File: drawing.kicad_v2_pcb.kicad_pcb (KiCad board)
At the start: 2 copper layers, 93 x 65 mm, 40 parts, among them IC1 DW01A-G, J1 Micro USB Chargeport, J2 Prog headers, J3 128x32 I2C OLED, J4 TP4056, J5 MK-12C02, J6 Conn_01x02, Q1 FS8205, U1 HT7333-SOT89, U2 ESP-12E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

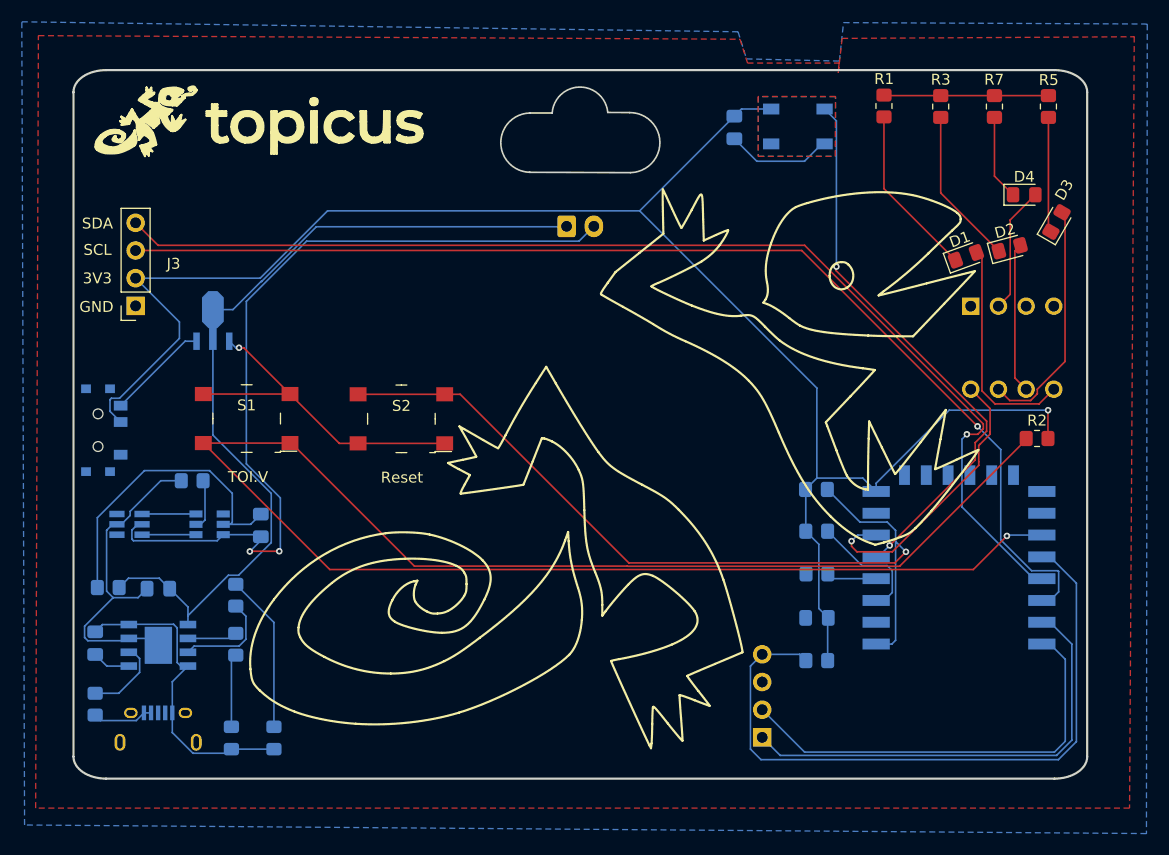
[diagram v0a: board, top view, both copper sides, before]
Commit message: Fixed HT7333 and charging circuit
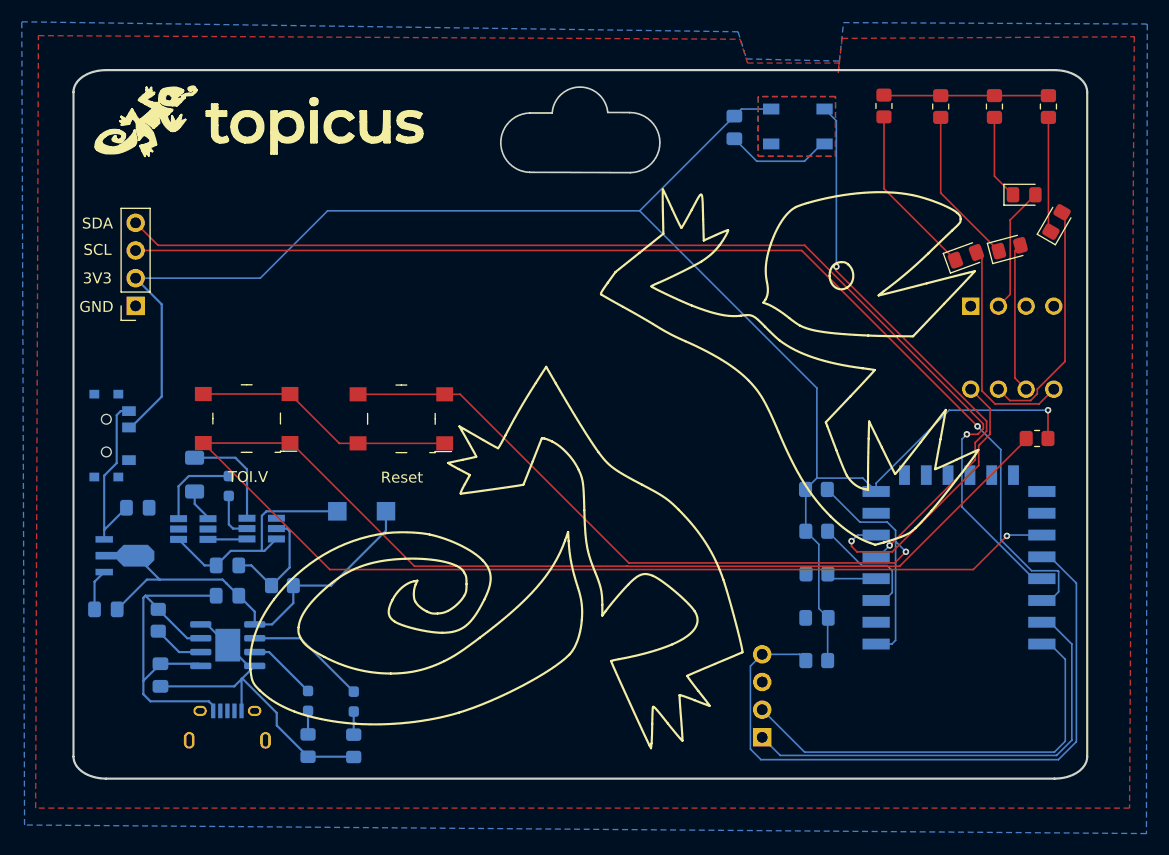
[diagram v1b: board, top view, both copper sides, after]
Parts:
- removed C2, C4: 0.1uF, Capacitor_SMD:C_0805_2012Metric_Pad1.18x1.45mm_HandSolder
- removed C5: 10uF, Capacitor_SMD:C_0805_2012Metric_Pad1.18x1.45mm_HandSolder
- removed D5: R-LED, LED_SMD:LED_0805_2012Metric_Pad1.15x1.40mm_HandSolder
- removed D6: G-LED, LED_SMD:LED_0805_2012Metric_Pad1.15x1.40mm_HandSolder
- removed IC1: DW01A-G, user-footprints:SOT95P280X135-6N
- removed J1: Micro USB Chargeport, digikey-footprints:USB_Micro_B_Female_10118194-0001LF
- removed J4: TP4056, Custom:SOIC127P600X175-9N
- removed J5: MK-12C02, user-footprints:MK12C02
- removed J6: Conn_01x02, Connector_JST:JST_EH_B2B-EH-A_1x02_P2.50mm_Vertical
- removed Q1: FS8205, user-footprints:FS8205
- removed R10, R12, R13: 1k, Resistor_SMD:R_0805_2012Metric_Pad1.20x1.40mm_HandSolder
- removed R11: 5k, Resistor_SMD:R_0805_2012Metric_Pad1.20x1.40mm_HandSolder
- removed R14: 100R, Resistor_SMD:R_0805_2012Metric_Pad1.20x1.40mm_HandSolder
- removed U1: HT7333-SOT89, Custom:Holtek-HT7333-SOT89-Level_A
- added C10: 10uF, Capacitor_SMD:C_0805_2012Metric_Pad1.18x1.45mm_HandSolder, B.Cu at (111.9, 101.6)
- added C6: 0.1uF, Capacitor_SMD:C_0805_2012Metric_Pad1.18x1.45mm_HandSolder, B.Cu at (114.0, 116.9)
- added C7: 10uF, Capacitor_SMD:C_0805_2012Metric_Pad1.18x1.45mm_HandSolder, B.Cu at (120.1, 109.7)
- added C8: 0.1uF, Capacitor_SMD:C_0805_2012Metric_Pad1.18x1.45mm_HandSolder, B.Cu at (120.1, 106.9)
- added C9: 10uF, Capacitor_SMD:C_0805_2012Metric_Pad1.18x1.45mm_HandSolder, B.Cu at (109.0, 110.9)
- added D8: RED, LED_SMD:LED_0805_2012Metric_Pad1.15x1.40mm_HandSolder, B.Cu at (127.5, 123.4)
- added D9: GREEN, LED_SMD:LED_0805_2012Metric_Pad1.15x1.40mm_HandSolder, B.Cu at (131.7, 123.4)
- added J10: Conn_01x01_Female, user-footprints:solderpad, B.Cu at (130.2, 101.9)
- added J12: Conn_01x01_Female, user-footprints:solderpad, B.Cu at (134.7, 101.9)
- added J14: MK-12C02, user-footprints:MK12C02, B.Cu at (109.0, 95.0)
- added J7: USB_B_Micro, digikey-footprints:USB_Micro_B_Female_10118194-0001LF, B.Cu at (120.1, 120.2)
- added R15: 1k, Resistor_SMD:R_0603_1608Metric_Pad0.98x0.95mm_HandSolder, B.Cu at (127.5, 119.3)
- added R16: 1k, Resistor_SMD:R_0603_1608Metric_Pad0.98x0.95mm_HandSolder, B.Cu at (131.7, 119.4)
- added R17: 10k, Resistor_SMD:R_0805_2012Metric_Pad1.20x1.40mm_HandSolder, B.Cu at (113.8, 111.9)
- added R18: 1k, Resistor_SMD:R_0603_1608Metric_Pad0.98x0.95mm_HandSolder, B.Cu at (120.3, 99.6)
- added R19: 0R, Resistor_SMD:R_1206_3216Metric_Pad1.30x1.75mm_HandSolder, B.Cu at (117.1, 98.5)
- added R20: 100, Resistor_SMD:R_0805_2012Metric_Pad1.20x1.40mm_HandSolder, B.Cu at (125.2, 108.7)
- added U4: TP4056, Package_SO:SOIC-8-1EP_3.9x4.9mm_P1.27mm_EP2.29x3mm, B.Cu at (120.2, 114.2)
- added U5: DW01, Package_TO_SOT_SMD:SOT-23-6_Handsoldering, B.Cu at (123.3, 103.5)
- added U6: FS8205A, Package_TO_SOT_SMD:SOT-23-6_Handsoldering, B.Cu at (117.0, 103.5)
- added U7: HT7333-SOT89, user-footprints:Holtek-HT7333-SOT89-Level_A, B.Cu at (110.8, 106.0)
- moved REF** 0.97 mm to (193.5, 66.6)
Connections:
- net +3V3 renamed +3.3V
- net GND renamed BAT-
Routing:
- net /Batt-: track 77.6 -> 0.00 mm, vias 2 -> 0
- net /Batt+: track 76.3 -> 0.00 mm
- net BAT+: track 0.00 -> 38.0 mm
- net VIN: track 0.00 -> 32.8 mm
- net /+5V: track 29.2 -> 0.00 mm
- net Net-(C4-Pad2): track 28.2 -> 0.00 mm
- net BAT-: track 96.5 -> 117.6 mm, vias 1 -> 0
- net Net-(J14-NO): track 0.00 -> 16.0 mm
- net Net-(D6-Pad1): track 14.5 -> 0.00 mm
- net Net-(U4-~{STDBY}): track 0.00 -> 11.1 mm
- net Net-(U5-VCC): track 0.00 -> 10.7 mm
- net /OC: track 0.00 -> 9.73 mm
- net Net-(J5-Pad3): track 9.41 -> 0.00 mm
- net Net-(J4-Pad7): track 9.24 -> 0.00 mm
- net Net-(J4-Pad2): track 7.37 -> 0.00 mm
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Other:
- copper layers 2 -> 4
- rule pad_to_mask_clearance: 0.0508 -> 0
- rule solder_mask_min_width: 0.25 -> 0.12
- board text added: "BAT+"
- board text added: "BAT-"

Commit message: Changed TH components to SMD
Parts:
- removed D7: Neopixel, user-footprints:LED_SK6812_PLCC4_5.0x5.0mm_P3.2mm_mirror
- removed the REF** at (193.5, 66.6)
- added D5: SK6812MINI, LED_SMD:LED_SK6812MINI_PLCC4_3.5x3.5mm_P1.75mm, B.Cu at (172.5, 66.6)
- added REF**: OSHW-Symbol_6.7x6mm_SilkScreen, Symbol:OSHW-Symbol_6.7x6mm_SilkScreen, B.Cu at (193.0, 66.6)
- U3: footprint digikey-footprints:DIP-8_W7.62mm -> Package_DIP:SMDIP-8_W7.62mm
- moved U3 4.32 mm to (191.4, 86.2), turned to 90 degrees
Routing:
- net Net-(D1-A): track 20.5 -> 4.71 mm, vias 0 -> 1
- net Net-(D3-A): track 22.1 -> 9.55 mm, vias 0 -> 1
- net Net-(D2-A): track 13.8 -> 5.99 mm, vias 0 -> 1
- net +3.3V: track 157.9 -> 165.5 mm
- net Net-(D4-A): track 11.6 -> 18.2 mm, vias 0 -> 1
- net BAT-: track 117.6 -> 112.0 mm
- net /LC: track 26.3 -> 31.0 mm, vias 1 -> 2
- net /NP: track 51.6 -> 49.4 mm

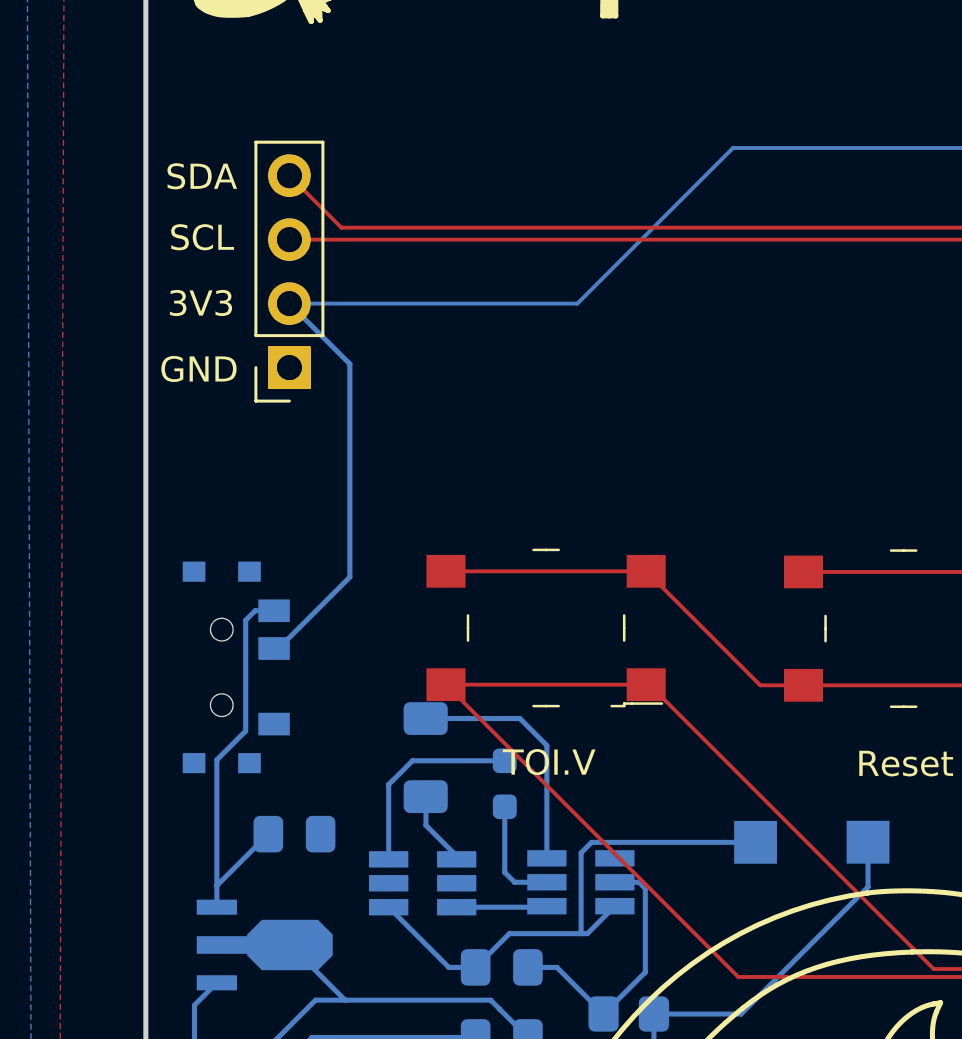
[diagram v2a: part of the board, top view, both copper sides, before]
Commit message: Added 3d models to renders
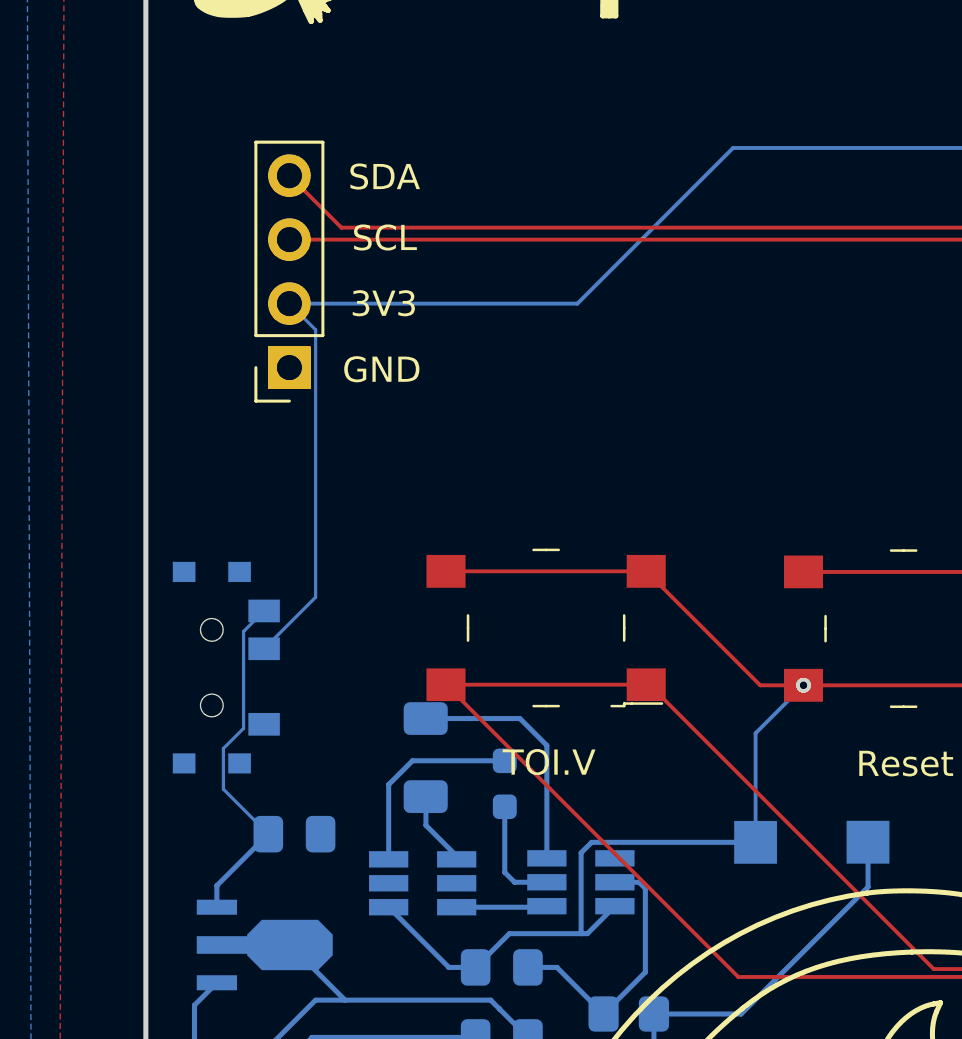
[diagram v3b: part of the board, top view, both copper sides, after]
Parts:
- removed REF**: OSHW-Symbol_6.7x6mm_SilkScreen, Symbol:OSHW-Symbol_6.7x6mm_SilkScreen
- moved J14 0.40 mm to (108.6, 95.0)
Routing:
- net BAT-: track 112.0 -> 119.0 mm, vias 0 -> 1
- net Net-(J14-NO): track 16.0 -> 14.0 mm
- net +3.3V: track 165.5 -> 164.4 mm
